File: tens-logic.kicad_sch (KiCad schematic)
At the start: 6 parts, among them U23 74AUC2G04, U24 74AUC2G04, U26 74AUC2G32, U27 74AUC2G32

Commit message: add : tens logic
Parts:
- removed unit 1 of U23
- added U1: 74AUC2G08, symbol 74xGxx:74AUC2G08
- added U2, U3: (no value), Package_TO_SOT_SMD:SOT-23-6, symbol CornetPrisme_Library:SN74LVC1G11
- added U4: 74AUC2G32, symbol 74xGxx:74AUC2G32
- added U5: 74AUC2G04, symbol 74xGxx:74AUC2G04
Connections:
- net a2: now also U3.1 (A), U5.1
- net b2: now also U2.3 (B)
- net c2: now also U2.6 (C)
- net d2: now also U1.1; no longer U25.12 (4A)
- net at U24.4, U28.3 (B): now also U3.3 (B)
- net at U24.6, U26.1: now also U1.2, U3.6 (C)
- net at U23.4: now also U25.12 (4A)
- net at U25.3 (1Y), U25.9 (3A), U26.6: now also U1.5
- new net: U2.1 (A), U5.6
- new net: U2.4 (Y), U4.1
- new net: U1.3, U4.5
- new net: U1.6, U1.7
- new net: U3.4 (Y), U4.2
- new net: U4.6, U4.7
- new net D_1: U4.3
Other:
- moved on the sheet: U23B, U23C, U24A, U24B, U24C, U26A, U26B, U26C, U27A, U27B, U27C

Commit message: add : alimentation
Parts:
- removed unit 3 of U1
- removed unit 2 of U2
- removed unit 3 of U26
- removed unit 3 of U27
- removed unit 2 of U28
- removed unit 3 of U4
- added C13, C14, C15, C16, C18, C19, C20, C21, C5: 0.1u, symbol Device:C
- added U32, U33: (no value), Package_TO_SOT_SMD:SOT-23-6, symbol CornetPrisme_Library:SN74LVC1G11
- added U43, U44, U45: 74AUC2G32, symbol 74xGxx:74AUC2G32
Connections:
- net +1V8: now reaches U25.14 (VCC)
- net +1V8: now also U23.5 (VCC), U24.5 (VCC), U3.5 (VCC), C13.2, C14.2, C15.2, C16.2, C18.2, C19.2, C20.2, C21.2, C5.2, U32.5 (VCC), U33.5 (VCC), U43.8 (VCC), U44.8 (VCC), U45.8 (VCC)
- net GND: now reaches U25.7 (GND)
- net GND: now also U23.2 (GND), U24.2 (GND), U3.2 (GND), C13.1, C14.1, C15.1, C16.1, C18.1, C19.1, C20.1, C21.1, C5.1, U32.2 (GND), U33.2 (GND), U43.4 (GND), U44.4 (GND), U45.4 (GND)
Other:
- moved on the sheet: U23C, U27A

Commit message: Branchement des pins
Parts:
- renumbered U24 to U23, U44 to U26, U45 to U27, U43 to U4, U24 to U5
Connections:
- no-connect marks 0 -> 3

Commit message: ajout composants
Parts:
- added C38, C40: 0.1u, symbol Device:C
- added unit 3 of U1
- added unit 2 of U2
- C13, C14, C15, C16, C18, C19, C20, C21, C5: Basic (none) -> Y; JLCPCB Part # (none) -> C1591; Manufacturer (none) -> Samsung Electro-Mechanics; Manufacturer Part Number (none) -> CL10B104KB8NNNC
- U1: Basic (none) -> X; JLCPCB Part # (none) -> C2860154; Manufacturer (none) -> TI; Manufacturer Part Number (none) -> SN74AUC2G08DCUR
- U2, U28, U3, U32, U33: Basic (none) -> X; JLCPCB Part # (none) -> C22046; Manufacturer (none) -> TI; Manufacturer Part Number (none) -> SN74LVC1G11DBVR
- U23, U5: Basic (none) -> X; JLCPCB Part # (none) -> C139318; Manufacturer (none) -> TI; Manufacturer Part Number (none) -> SN74AUP2G14DCKR
- U25: Basic (none) -> X; JLCPCB Part # (none) -> C2868761; Manufacturer (none) -> TI; Manufacturer Part Number (none) -> SN74ALVC08DR
- U26, U27, U4: Basic (none) -> X; JLCPCB Part # (none) -> C2876519; Manufacturer (none) -> TI; Manufacturer Part Number (none) -> SN74AUP2G32DCUR
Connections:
- net +1V8: now also C38.2, C40.2, U1.8 (VCC), U2.5 (VCC)
- net GND: now also C38.1, C40.1, U1.4 (GND), U2.2 (GND)

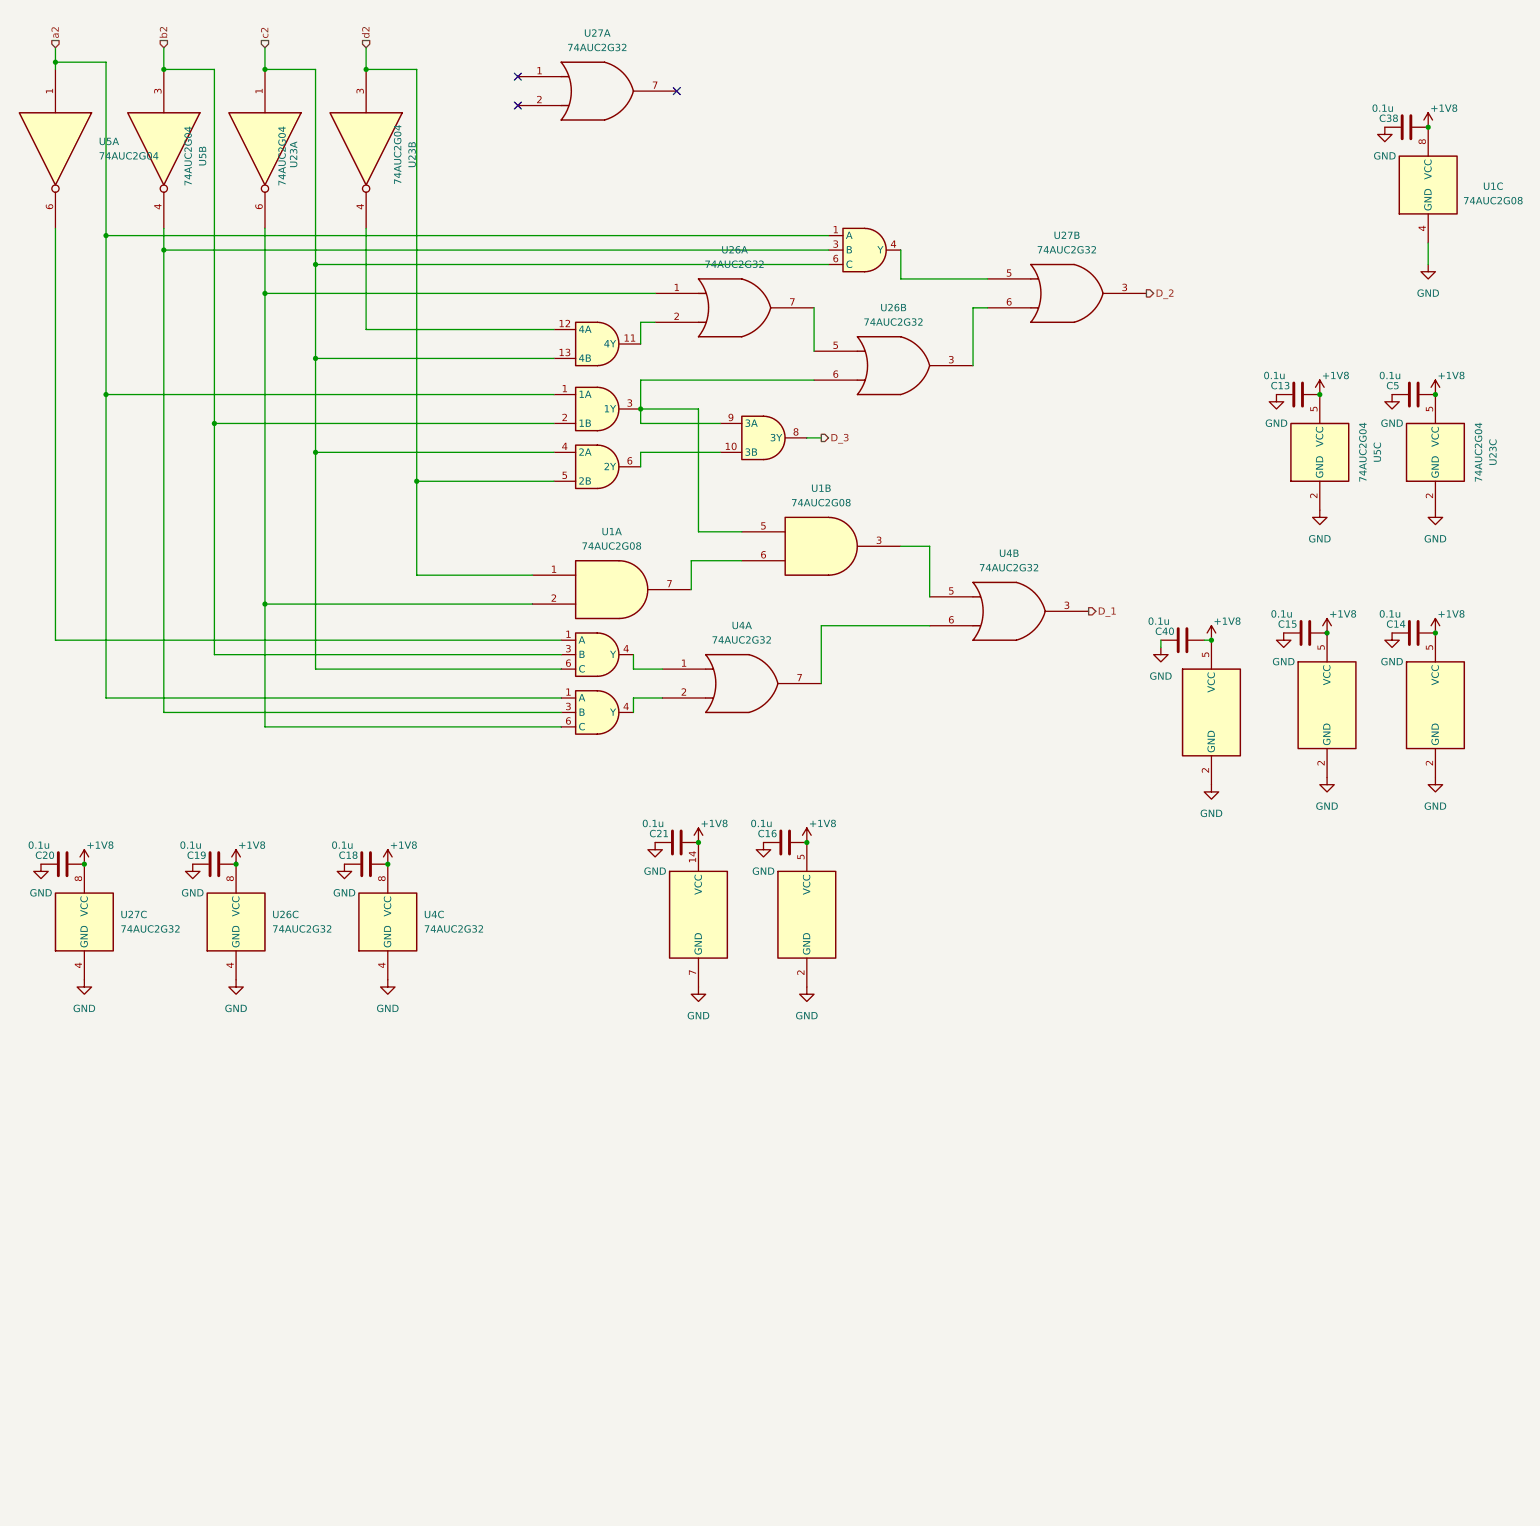
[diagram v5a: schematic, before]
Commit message: elimination of the error in the logic of the tens place
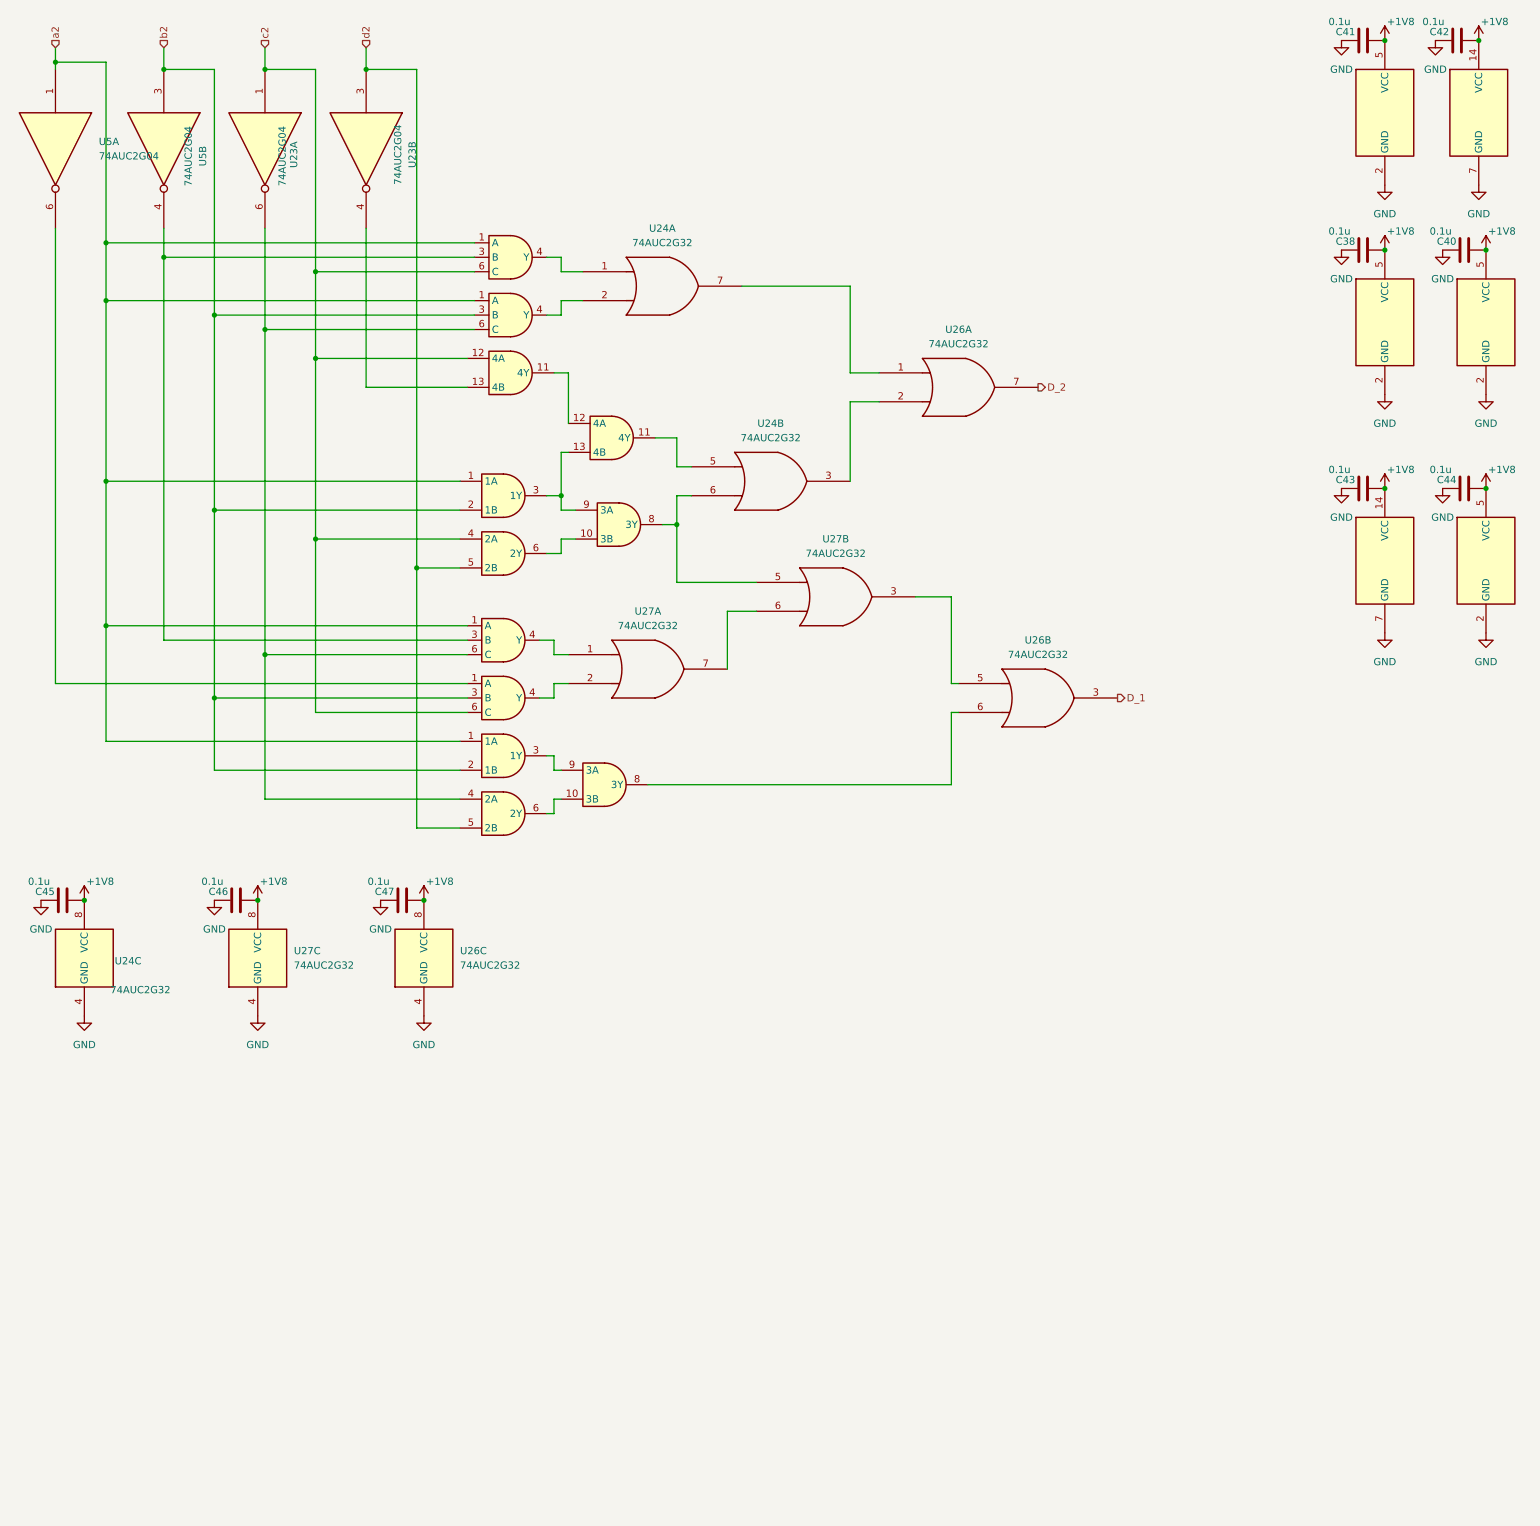
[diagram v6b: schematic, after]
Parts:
- removed C13, C14, C15, C16, C18, C19, C20, C21, C5: 0.1u, symbol Device:C
- removed U1: 74AUC2G08, symbol 74xGxx:74AUC2G08
- removed unit 3 of U23
- removed U28, U32, U33: (no value), Package_TO_SOT_SMD:SOT-23-6, symbol CornetPrisme_Library:SN74LVC1G11
- removed U4: 74AUC2G32, symbol 74xGxx:74AUC2G32
- removed unit 3 of U5
- added C41, C42, C43, C44, C45, C46, C47: 0.1u, symbol Device:C
- added U1, U4: (no value), Package_TO_SOT_SMD:SOT-23-6, symbol CornetPrisme_Library:SN74LVC1G11
- added U24: 74AUC2G32, symbol 74xGxx:74AUC2G32
- added U8: (no value), Package_SO:SOIC-14_3.9x8.7mm_P1.27mm, symbol CornetPrisme_Library:SN74ALVC08
- U2, U3: Basic X -> (none); JLCPCB Part # C22046 -> (none); Manufacturer TI -> (none); Manufacturer Part Number SN74LVC1G11DBVR -> (none)
- U26, U27: Basic X -> (none); JLCPCB Part # C2876519 -> (none); Manufacturer TI -> (none); Manufacturer Part Number SN74AUP2G32DCUR -> (none)
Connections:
- net D_3 is gone; now on an unnamed net: U25.8 (3Y)
- net +1V8: now also C41.2, C42.2, C43.2, C44.2, C45.2, C46.2, C47.2, U1.5 (VCC), U24.8 (VCC), U4.5 (VCC), U8.14 (VCC)
- net D_1: now also U26.3
- net D_2: now also U26.7; no longer U27.3
- net GND: now also C41.1, C42.1, C43.1, C44.1, C45.1, C46.1, C47.1, U1.2 (GND), U24.4 (GND), U4.2 (GND), U8.7 (GND)
- net a2: now also U2.1 (A), U1.1 (A), U8.1 (1A)
- net b2: now also U1.3 (B), U4.3 (B), U8.2 (1B); no longer U2.3 (B)
- net c2: now also U25.12 (4A), U4.6 (C); no longer U25.13 (4B)
- net d2: now also U8.5 (2B)
- net at U5.6: now also U4.1 (A); no longer U2.1 (A)
- net at U2.4 (Y): now also U24.1
- net at U3.3 (B), U5.4: now also U2.3 (B)
- net at U27.1: now also U3.4 (Y)
- net at U27.2: now also U4.4 (Y)
- net at U27.7: now also U27.6
- net at U25.3 (1Y), U25.9 (3A): now also U8.13 (4B); no longer U26.6
- net at U23.6, U3.6 (C): now also U1.6 (C), U8.4 (2A); no longer U26.1
- net at U23.4: now also U25.13 (4B); no longer U25.12 (4A)
- net at U27.5: now also U24.6
- net at U26.2: now also U24.3; no longer U25.11 (4Y)
- net at U26.5: now also U27.3; no longer U26.7
- new net: U24.7, U26.1
- new net: U25.11 (4Y), U8.12 (4A)
- new net: U24.5, U8.11 (4Y)
- new net: U8.10 (3B), U8.6 (2Y)
- new net: U26.6, U8.8 (3Y)
- new net: U8.3 (1Y), U8.9 (3A)
- new net: U1.4 (Y), U24.2
- no-connect marks 3 -> 0

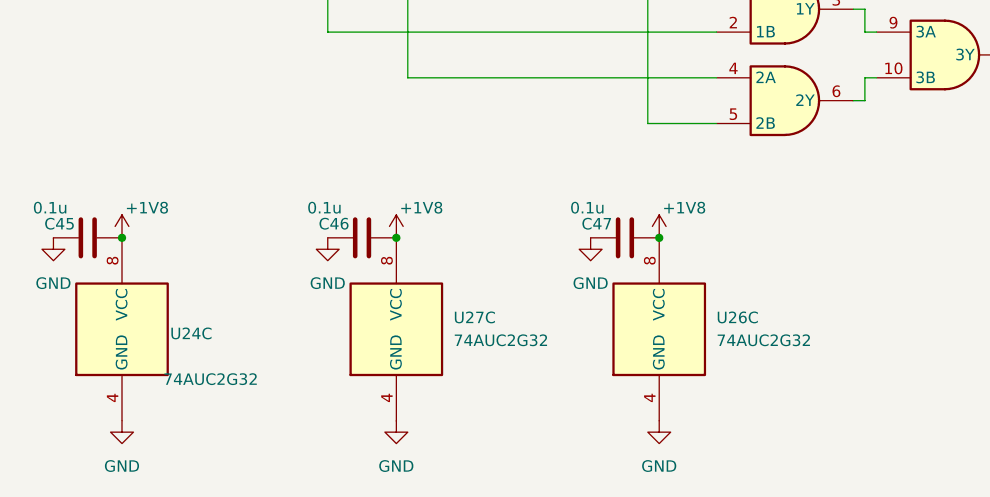
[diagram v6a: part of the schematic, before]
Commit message: elimination of errors
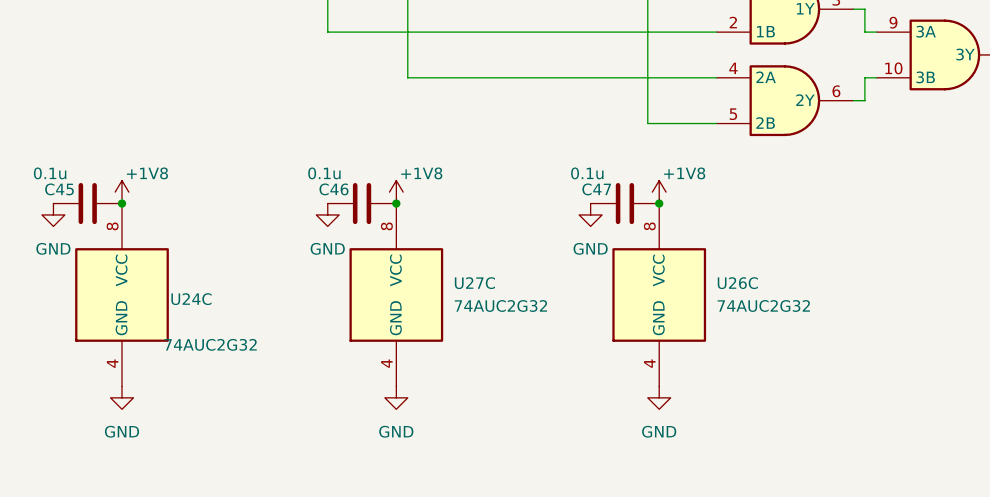
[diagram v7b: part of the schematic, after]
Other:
- moved on the sheet: C45, C46, C47, U24C, U26C, U27C

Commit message: add footprint
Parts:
- added C48, C49: 0.1u, Capacitor_SMD:C_0603_1608Metric, symbol Device:C
- added unit 3 of U23
- added unit 3 of U5
- C38, C40, C41, C42, C43, C44, C45, C46, C47: footprint (none) -> Capacitor_SMD:C_0603_1608Metric
- U1, U2, U3, U4: Basic (none) -> X; JLCPCB Part # (none) -> C22046; Manufacturer (none) -> TI; Manufacturer Part Number (none) -> SN74LVC1G11DBVR
- U23, U5: footprint (none) -> Package_TO_SOT_SMD:Texas_R-PDSO-G6
- U24, U26, U27: value 74AUC2G32 -> ²; footprint (none) -> Package_SO:VSSOP-8_3x3mm_P0.65mm; Basic (none) -> X; JLCPCB Part # (none) -> C2876519; Manufacturer (none) -> TI; Manufacturer Part Number (none) -> SN74AUP2G32DCUR
- U8: Basic (none) -> X; JLCPCB Part # (none) -> C2868761; Manufacturer (none) -> TI; Manufacturer Part Number (none) -> SN74ALVC08DR
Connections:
- net +1V8: now also C48.2, C49.2, U23.5 (VCC), U5.5 (VCC)
- net GND: now also C48.1, C49.1, U23.2 (GND), U5.2 (GND)
